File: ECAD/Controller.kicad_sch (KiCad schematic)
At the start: 6 parts, among them SW1 SW_Push, U4 ESP32-WROOM-32

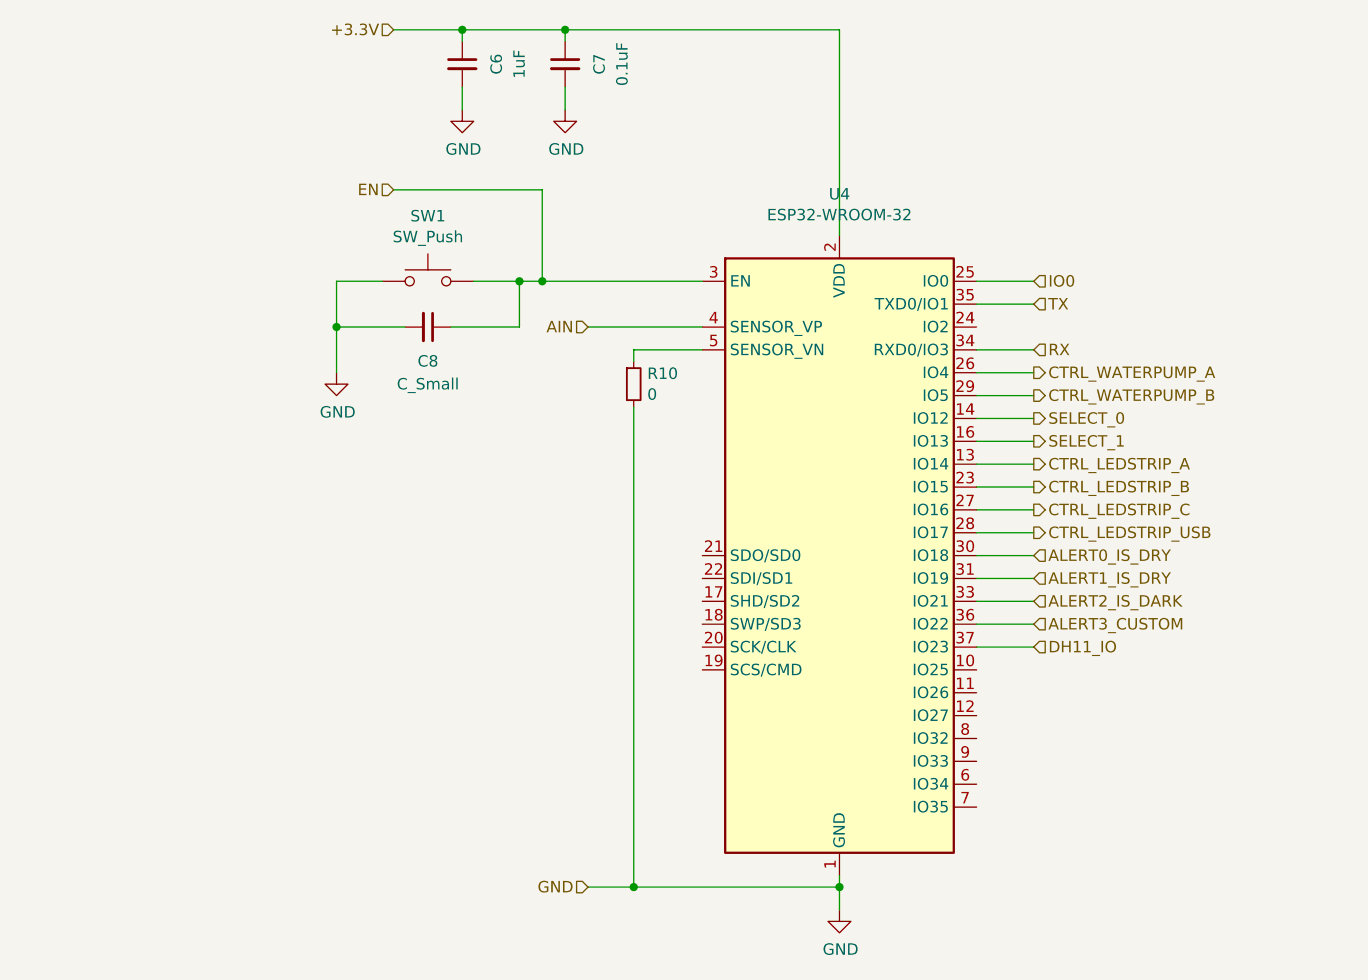
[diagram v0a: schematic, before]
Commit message: finishing up pcb, only billonly bill of materials need to be done to be compatible with lc from jlcpcb
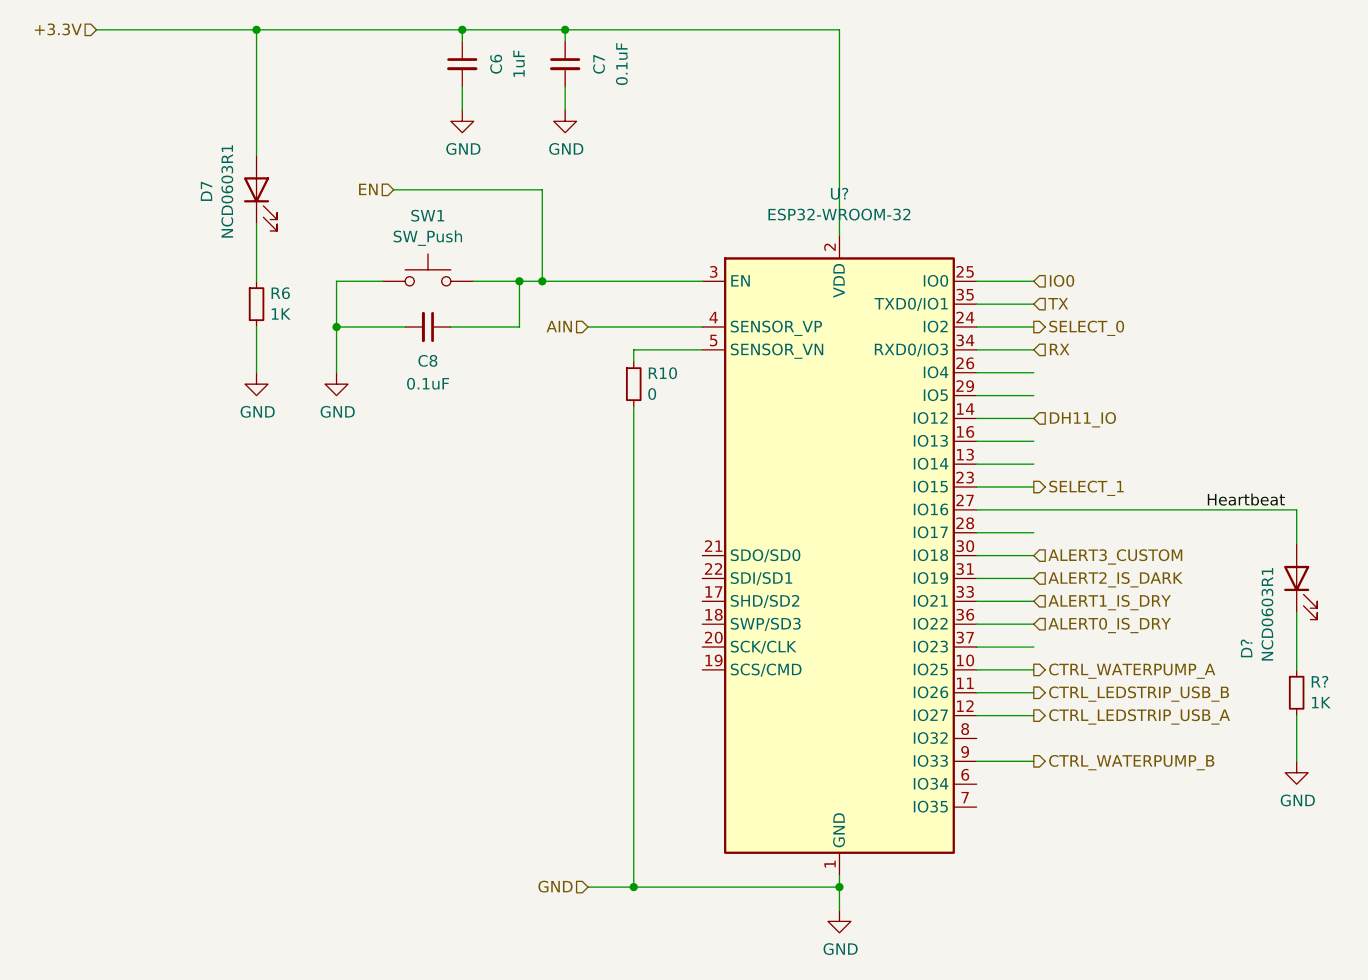
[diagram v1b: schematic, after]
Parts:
- removed U4: ESP32-WROOM-32, RF_Module:ESP32-WROOM-32, symbol RF_Module:ESP32-WROOM-32
- added D7, D?: NCD0603R1, LED_SMD:LED_0603_1608Metric, symbol Device:LED
- added R6, R?: 1K, Resistor_SMD:R_0603_1608Metric, symbol Device:R_Small
- added U?: ESP32-WROOM-32, RF_Module:ESP32-WROOM-32, symbol RF_Module:ESP32-WROOM-32
- C8: value C_Small -> 0.1uF
- SW1: footprint Potentiometer_SMD:Potentiometer_Bourns_TC33X_Vertical -> Button_Switch_THT:SW_PUSH_6mm_H4.3mm
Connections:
- net +3.3V: now also D7.2 (A), U?.2 (VDD)
- net AIN: now also U?.4 (SENSOR_VP)
- net ALERT0_IS_DRY: now also U?.36 (IO22)
- net ALERT1_IS_DRY: now also U?.33 (IO21)
- net ALERT2_IS_DARK: now also U?.31 (IO19)
- net ALERT3_CUSTOM: now also U?.30 (IO18)
- net CTRL_WATERPUMP_A: now also U?.10 (IO25)
- net CTRL_WATERPUMP_B: now also U?.9 (IO33)
- net DH11_IO: now also U?.14 (IO12)
- net EN: now also U?.3 (EN)
- net GND: now also R6.2, R?.2, U?.1 (GND), U?.15 (GND), U?.38 (GND), U?.39 (GND)
- net IO0: now also U?.25 (IO0)
- net RX: now also U?.34 (RXD0/IO3)
- net SELECT_0: now also U?.24 (IO2)
- net SELECT_1: now also U?.23 (IO15)
- net TX: now also U?.35 (TXD0/IO1)
- net at R10.1: now also U?.5 (SENSOR_VN)
- new net: D?.1 (K), R?.1
- new net: D7.1 (K), R6.1
- new net CTRL_LEDSTRIP_USB_A: U?.12 (IO27)
- new net CTRL_LEDSTRIP_USB_B: U?.11 (IO26)
- new net Heartbeat: D?.2 (A), U?.27 (IO16)

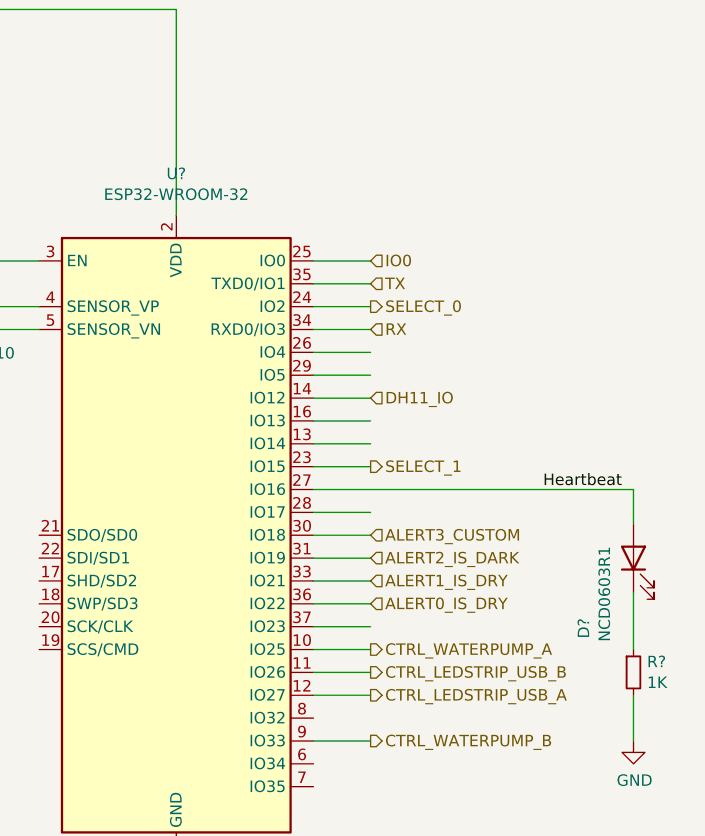
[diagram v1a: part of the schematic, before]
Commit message: BOM fixed, ready to order
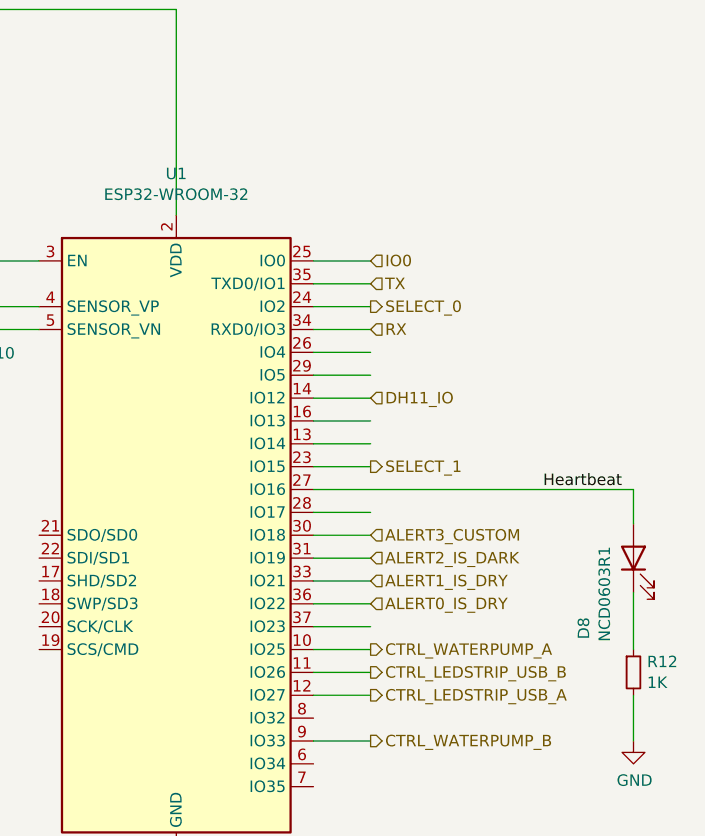
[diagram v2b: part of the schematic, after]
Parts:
- C6: Manufacturer (none) -> Samsung Electro-Mechanics; Manufacturer Number (none) -> CL10A105KO8NNNC
- C7, C8: Manufacturer (none) -> CCTC; Manufacturer Number (none) -> TCC0603X7R104K500CT
- D7: Manufacturer (none) -> Foshan NationStar Optoelectronics; Manufacturer Number (none) -> NCD0603R1
- D8: renamed from D?; Manufacturer (none) -> Foshan NationStar Optoelectronics; Manufacturer Number (none) -> NCD0603R1
- R12: renamed from R?; Manufacturer (none) -> FH(Guangdong Fenghua Advanced Tech); Manufacturer Number (none) -> RS-03K1001FT
- R6: Manufacturer (none) -> FH(Guangdong Fenghua Advanced Tech); Manufacturer Number (none) -> RS-03K1001FT
- SW1: Manufacturer (none) -> XUNPU; Manufacturer Number (none) -> TS-1002-04326
- U1: renamed from U?; Manufacturer (none) -> Espressif Systems; Manufacturer Number (none) -> ESP32-WROOM-32
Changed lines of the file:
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@@
   (symbol (lib_id "power:GND") (at 200.66 107.95 0) (unit 1)
     (in_bom yes) (on_board yes)
-    (property "Reference" "#PWR?" (id 0) (at 200.66 114.3 0)
+    (property "Reference" "#PWR0153" (id 0) (at 200.66 114.3 0)
       (effects (font (size 1.27 1.27)) hide)
     )
@@
       (effects (font (size 1.27 1.27)) hide)
     )
-    (property "Datasheet" "~" (id 3) (at 85.09 57.15 0)
+    (property "Datasheet" "https://datasheet.lcsc.com/lcsc/1811011704_FH-Guangdong-Fenghua-Advanced-Tech-RS-03K1001FT_C115325.pdf" (id 3) (at 85.09 57.15 0)
+      (effects (font (size 1.27 1.27)) hide)
+    )
+    (property "Manufacturer" "FH(Guangdong Fenghua Advanced Tech)" (id 4) (at 85.09 57.15 0)
+      (effects (font (size 1.27 1.27)) hide)
+    )
+    (property "Manufacturer Number" "RS-03K1001FT" (id 5) (at 85.09 57.15 0)
       (effects (font (size 1.27 1.27)) hide)
     )
@@
   (symbol (lib_id "Device:R_Small") (at 200.66 100.33 0) (unit 1)
     (in_bom yes) (on_board yes)
-    (property "Reference" "R?" (id 0) (at 202.1586 99.1616 0)
+    (property "Reference" "R12" (id 0) (at 202.1586 99.1616 0)
       (effects (font (size 1.27 1.27)) (justify left))
     )
@@
       (effects (font (size 1.27 1.27)) hide)
     )
-    (property "Datasheet" "~" (id 3) (at 200.66 100.33 0)
+    (property "Datasheet" "https://datasheet.lcsc.com/lcsc/1811011704_FH-Guangdong-Fenghua-Advanced-Tech-RS-03K1001FT_C115325.pdf" (id 3) (at 200.66 100.33 0)
+      (effects (font (size 1.27 1.27)) hide)
+    )
+    (property "Manufacturer" "FH(Guangdong Fenghua Advanced Tech)" (id 4) (at 200.66 100.33 0)
+      (effects (font (size 1.27 1.27)) hide)
+    )
+    (property "Manufacturer Number" "RS-03K1001FT" (id 5) (at 200.66 100.33 0)
       (effects (font (size 1.27 1.27)) hide)
     )
@@
       (effects (font (size 1.27 1.27)) hide)
     )
-    (property "Datasheet" "~" (id 3) (at 104.14 59.69 0)
+    (property "Datasheet" "https://datasheet.lcsc.com/lcsc/1810181652_CCTC-TCC0603X7R104K500CT_C282519.pdf" (id 3) (at 104.14 59.69 0)
+      (effects (font (size 1.27 1.27)) hide)
+    )
+    (property "Manufacturer" "CCTC" (id 4) (at 104.14 59.69 0)
+      (effects (font (size 1.27 1.27)) hide)
+    )
+    (property "Manufacturer Number" "TCC0603X7R104K500CT" (id 5) (at 104.14 59.69 0)
       (effects (font (size 1.27 1.27)) hide)
     )
@@
       (effects (font (size 1.27 1.27)) hide)
     )
-    (property "Datasheet" "~" (id 3) (at 107.95 30.48 0)
+    (property "Datasheet" "https://datasheet.lcsc.com/lcsc/1811021622_Samsung-Electro-Mechanics-CL10A105KO8NNNC_C1592.pdf" (id 3) (at 107.95 30.48 0)
+      (effects (font (size 1.27 1.27)) hide)
+    )
+    (property "Manufacturer" "Samsung Electro-Mechanics" (id 4) (at 107.95 30.48 0)
+      (effects (font (size 1.27 1.27)) hide)
+    )
+    (property "Manufacturer Number" "CL10A105KO8NNNC" (id 5) (at 107.95 30.48 0)
       (effects (font (size 1.27 1.27)) hide)
     )
@@
       (effects (font (size 1.27 1.27)) hide)
     )
-    (property "Datasheet" "~" (id 3) (at 119.38 30.48 0)
+    (property "Datasheet" "https://datasheet.lcsc.com/lcsc/1810181652_CCTC-TCC0603X7R104K500CT_C282519.pdf" (id 3) (at 119.38 30.48 0)
+      (effects (font (size 1.27 1.27)) hide)
+    )
+    (property "Manufacturer" "CCTC" (id 4) (at 119.38 30.48 0)
+      (effects (font (size 1.27 1.27)) hide)
+    )
+    (property "Manufacturer Number" "TCC0603X7R104K500CT" (id 5) (at 119.38 30.48 0)
       (effects (font (size 1.27 1.27)) hide)
     )
@@
       (effects (font (size 1.27 1.27)) hide)
     )
-    (property "Datasheet" "~" (id 3) (at 85.09 44.45 0)
+    (property "Datasheet" "https://datasheet.lcsc.com/lcsc/2008201032_Foshan-NationStar-Optoelectronics-NCD0603R1_C84263.pdf" (id 3) (at 85.09 44.45 0)
+      (effects (font (size 1.27 1.27)) hide)
+    )
+    (property "Manufacturer" "	Foshan NationStar Optoelectronics" (id 4) (at 85.09 44.45 0)
+      (effects (font (size 1.27 1.27)) hide)
+    )
+    (property "Manufacturer Number" "NCD0603R1" (id 5) (at 85.09 44.45 0)
       (effects (font (size 1.27 1.27)) hide)
     )
@@
   (symbol (lib_id "Device:LED") (at 200.66 87.63 90) (unit 1)
     (in_bom yes) (on_board yes)
-    (property "Reference" "D?" (id 0) (at 195.1482 95.4278 0))
+    (property "Reference" "D8" (id 0) (at 195.1482 95.4278 0))
     (property "Value" "NCD0603R1" (id 1) (at 197.4596 91.6178 0))
     (property "Footprint" "LED_SMD:LED_0603_1608Metric" (id 2) (at 200.66 87.63 0)
       (effects (font (size 1.27 1.27)) hide)
     )
-    (property "Datasheet" "~" (id 3) (at 200.66 87.63 0)
+    (property "Datasheet" "https://datasheet.lcsc.com/lcsc/2008201032_Foshan-NationStar-Optoelectronics-NCD0603R1_C84263.pdf" (id 3) (at 200.66 87.63 0)
+      (effects (font (size 1.27 1.27)) hide)
+    )
+    (property "Manufacturer" "	Foshan NationStar Optoelectronics" (id 4) (at 200.66 87.63 0)
+      (effects (font (size 1.27 1.27)) hide)
+    )
+    (property "Manufacturer Number" "NCD0603R1" (id 5) (at 200.66 87.63 0)
       (effects (font (size 1.27 1.27)) hide)
     )
@@
       (effects (font (size 1.27 1.27)) hide)
     )
-    (property "Datasheet" "~" (id 3) (at 104.14 49.53 0)
+    (property "Datasheet" "~https://datasheet.lcsc.com/lcsc/1911212104_XUNPU-TS-1002-04326_C455089.pdf" (id 3) (at 104.14 49.53 0)
+      (effects (font (size 1.27 1.27)) hide)
+    )
+    (property "Manufacturer" "XUNPU" (id 4) (at 104.14 54.61 0)
+      (effects (font (size 1.27 1.27)) hide)
+    )
+    (property "Manufacturer Number" "TS-1002-04326" (id 5) (at 104.14 54.61 0)
       (effects (font (size 1.27 1.27)) hide)
     )
@@
   (symbol (lib_id "RF_Module:ESP32-WROOM-32") (at 149.86 85.09 0) (unit 1)
     (in_bom yes) (on_board yes)
-    (property "Reference" "U?" (id 0) (at 149.86 44.9326 0))
+    (property "Reference" "U1" (id 0) (at 149.86 44.9326 0))
     (property "Value" "ESP32-WROOM-32" (id 1) (at 149.86 47.244 0))
     (property "Footprint" "RF_Module:ESP32-WROOM-32" (id 2) (at 149.86 123.19 0)
@@
       (effects (font (size 1.27 1.27)) hide)
     )
+    (property "Manufacturer" "Espressif Systems" (id 4) (at 149.86 85.09 0)
+      (effects (font (size 1.27 1.27)) hide)
+    )
+    (property "Manufacturer Number" "	ESP32-WROOM-32" (id 5) (at 149.86 85.09 0)
+      (effects (font (size 1.27 1.27)) hide)
+    )

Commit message: adding production and step files
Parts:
- C6: Manufacturer Samsung Electro-Mechanics -> Samsung Electro-Mechanics; Package (none) -> 0603
- C7, C8, D7, D8, R10, R12, R6: Package (none) -> 0603
- SW1: Package (none) -> Through Hole,6x6x4.3mm
- U1: Package (none) -> WIFI Module
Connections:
- net CTRL_WATERPUMP_B: now also U1.13 (IO14); no longer U1.9 (IO33)
- net SCL: now reaches U1.8 (IO32)
- net DH11_IO: no longer names the net of U1.14 (IO12)
- new net SDA: U1.9 (IO33)
- no-connect marks 0 -> 15
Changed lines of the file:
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@@
   (junction (at 127 121.92) (diameter 0.9144) (color 0 0 0 0))
   (junction (at 149.86 121.92) (diameter 0.9144) (color 0 0 0 0))
+  (no_connect (at 134.62 85.09))
+  (no_connect (at 134.62 87.63))
+  (no_connect (at 134.62 90.17))
+  (no_connect (at 134.62 92.71))
+  (no_connect (at 134.62 95.25))
+  (no_connect (at 134.62 97.79))
+  (no_connect (at 165.1 64.77))
+  (no_connect (at 165.1 67.31))
+  (no_connect (at 165.1 69.85))
+  (no_connect (at 165.1 72.39))
+  (no_connect (at 165.1 82.55))
+  (no_connect (at 165.1 95.25))
+  (no_connect (at 165.1 110.49))
+  (no_connect (at 165.1 113.03))
+  (no_connect (at 200.66 105.41))
   (wire (pts (xy 67.31 26.67) (xy 85.09 26.67))
     (stroke (width 0) (type solid) (color 0 0 0 0))
@@
     (stroke (width 0) (type solid) (color 0 0 0 0))
   )
-  (wire (pts (xy 165.1 64.77) (xy 171.45 64.77))
-    (stroke (width 0) (type solid) (color 0 0 0 0))
-  )
-  (wire (pts (xy 165.1 67.31) (xy 171.45 67.31))
-    (stroke (width 0) (type solid) (color 0 0 0 0))
-  )
-  (wire (pts (xy 165.1 69.85) (xy 171.45 69.85))
-    (stroke (width 0) (type solid) (color 0 0 0 0))
-  )
-  (wire (pts (xy 165.1 72.39) (xy 171.45 72.39))
-    (stroke (width 0) (type solid) (color 0 0 0 0))
-  )
   (wire (pts (xy 165.1 74.93) (xy 171.45 74.93))
     (stroke (width 0) (type solid) (color 0 0 0 0))
@@
     (stroke (width 0) (type solid) (color 0 0 0 0))
   )
-  (wire (pts (xy 165.1 82.55) (xy 171.45 82.55))
-    (stroke (width 0) (type solid) (color 0 0 0 0))
-  )
   (wire (pts (xy 165.1 85.09) (xy 171.45 85.09))
     (stroke (width 0) (type solid) (color 0 0 0 0))
@@
     (stroke (width 0) (type solid) (color 0 0 0 0))
   )
-  (wire (pts (xy 165.1 95.25) (xy 171.45 95.25))
-    (stroke (width 0) (type solid) (color 0 0 0 0))
-  )
   (wire (pts (xy 165.1 97.79) (xy 171.45 97.79))
     (stroke (width 0) (type solid) (color 0 0 0 0))
@@
   )
   (wire (pts (xy 165.1 102.87) (xy 171.45 102.87))
+    (stroke (width 0) (type solid) (color 0 0 0 0))
+  )
+  (wire (pts (xy 165.1 105.41) (xy 171.45 105.41))
     (stroke (width 0) (type solid) (color 0 0 0 0))
   )
@@
     (effects (font (size 1.27 1.27)) (justify left))
   )
-  (hierarchical_label "TX" (shape input) (at 171.45 57.15 0)
+  (hierarchical_label "TX" (shape output) (at 171.45 57.15 0)
     (effects (font (size 1.27 1.27)) (justify left))
   )
@@
     (effects (font (size 1.27 1.27)) (justify left))
   )
-  (hierarchical_label "DH11_IO" (shape input) (at 171.45 69.85 0)
+  (hierarchical_label "CTRL_WATERPUMP_B" (shape output) (at 171.45 74.93 0)
     (effects (font (size 1.27 1.27)) (justify left))
   )
@@
     (effects (font (size 1.27 1.27)) (justify left))
   )
-  (hierarchical_label "CTRL_WATERPUMP_B" (shape output) (at 171.45 107.95 0)
+  (hierarchical_label "SCL" (shape output) (at 171.45 105.41 0)
+    (effects (font (size 1.27 1.27)) (justify left))
+  )
+  (hierarchical_label "SDA" (shape bidirectional) (at 171.45 107.95 0)
     (effects (font (size 1.27 1.27)) (justify left))
   )
@@
       (effects (font (size 1.27 1.27)) hide)
     )
+    (property "Package" "0603" (id 4) (at 85.09 57.15 0)
+      (effects (font (size 1.27 1.27)) hide)
+    )
     (pin "1")
     (pin "2")
@@
       (effects (font (size 1.27 1.27)) hide)
     )
+    (property "Package" "0603" (id 4) (at 127 66.04 0)
+      (effects (font (size 1.27 1.27)) hide)
+    )
     (pin "1")
     (pin "2")
@@
     )
     (property "Manufacturer Number" "RS-03K1001FT" (id 5) (at 200.66 100.33 0)
+      (effects (font (size 1.27 1.27)) hide)
+    )
+    (property "Package" "0603" (id 4) (at 200.66 100.33 0)
       (effects (font (size 1.27 1.27)) hide)
     )
@@
       (effects (font (size 1.27 1.27)) hide)
     )
+    (property "Package" "0603" (id 4) (at 104.14 59.69 0)
+      (effects (font (size 1.27 1.27)) hide)
+    )
     (pin "1")
     (pin "2")
@@
       (effects (font (size 1.27 1.27)) hide)
     )
-    (property "Manufacturer" "Samsung Electro-Mechanics" (id 4) (at 107.95 30.48 0)
+    (property "Manufacturer" "	Samsung Electro-Mechanics" (id 4) (at 107.95 30.48 0)
       (effects (font (size 1.27 1.27)) hide)
     )
     (property "Manufacturer Number" "CL10A105KO8NNNC" (id 5) (at 107.95 30.48 0)
+      (effects (font (size 1.27 1.27)) hide)
+    )
+    (property "Package" "0603" (id 4) (at 107.95 30.48 0)
       (effects (font (size 1.27 1.27)) hide)
     )
@@
       (effects (font (size 1.27 1.27)) hide)
     )
+    (property "Package" "0603" (id 4) (at 119.38 30.48 0)
+      (effects (font (size 1.27 1.27)) hide)
+    )
     (pin "1")
     (pin "2")
@@
       (effects (font (size 1.27 1.27)) hide)
     )
+    (property "Package" "0603" (id 4) (at 85.09 44.45 0)
+      (effects (font (size 1.27 1.27)) hide)
+    )
     (pin "1")
     (pin "2")
@@
       (effects (font (size 1.27 1.27)) hide)
     )
+    (property "Package" "0603" (id 4) (at 200.66 87.63 0)
+      (effects (font (size 1.27 1.27)) hide)
+    )
     (pin "1")
     (pin "2")
@@
       (effects (font (size 1.27 1.27)) hide)
     )
+    (property "Package" "Through Hole,6x6x4.3mm" (id 4) (at 104.14 54.61 0)
+      (effects (font (size 1.27 1.27)) hide)
+    )
     (pin "1")
     (pin "2")
@@
       (effects (font (size 1.27 1.27)) hide)
     )
+    (property "Package" "WIFI Module" (id 4) (at 149.86 85.09 0)
+      (effects (font (size 1.27 1.27)) hide)
+    )
